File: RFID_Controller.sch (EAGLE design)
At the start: 25 parts, among them IC1 74HC595N, K1 FTR-K1C, T1 BC547, T2 BC547

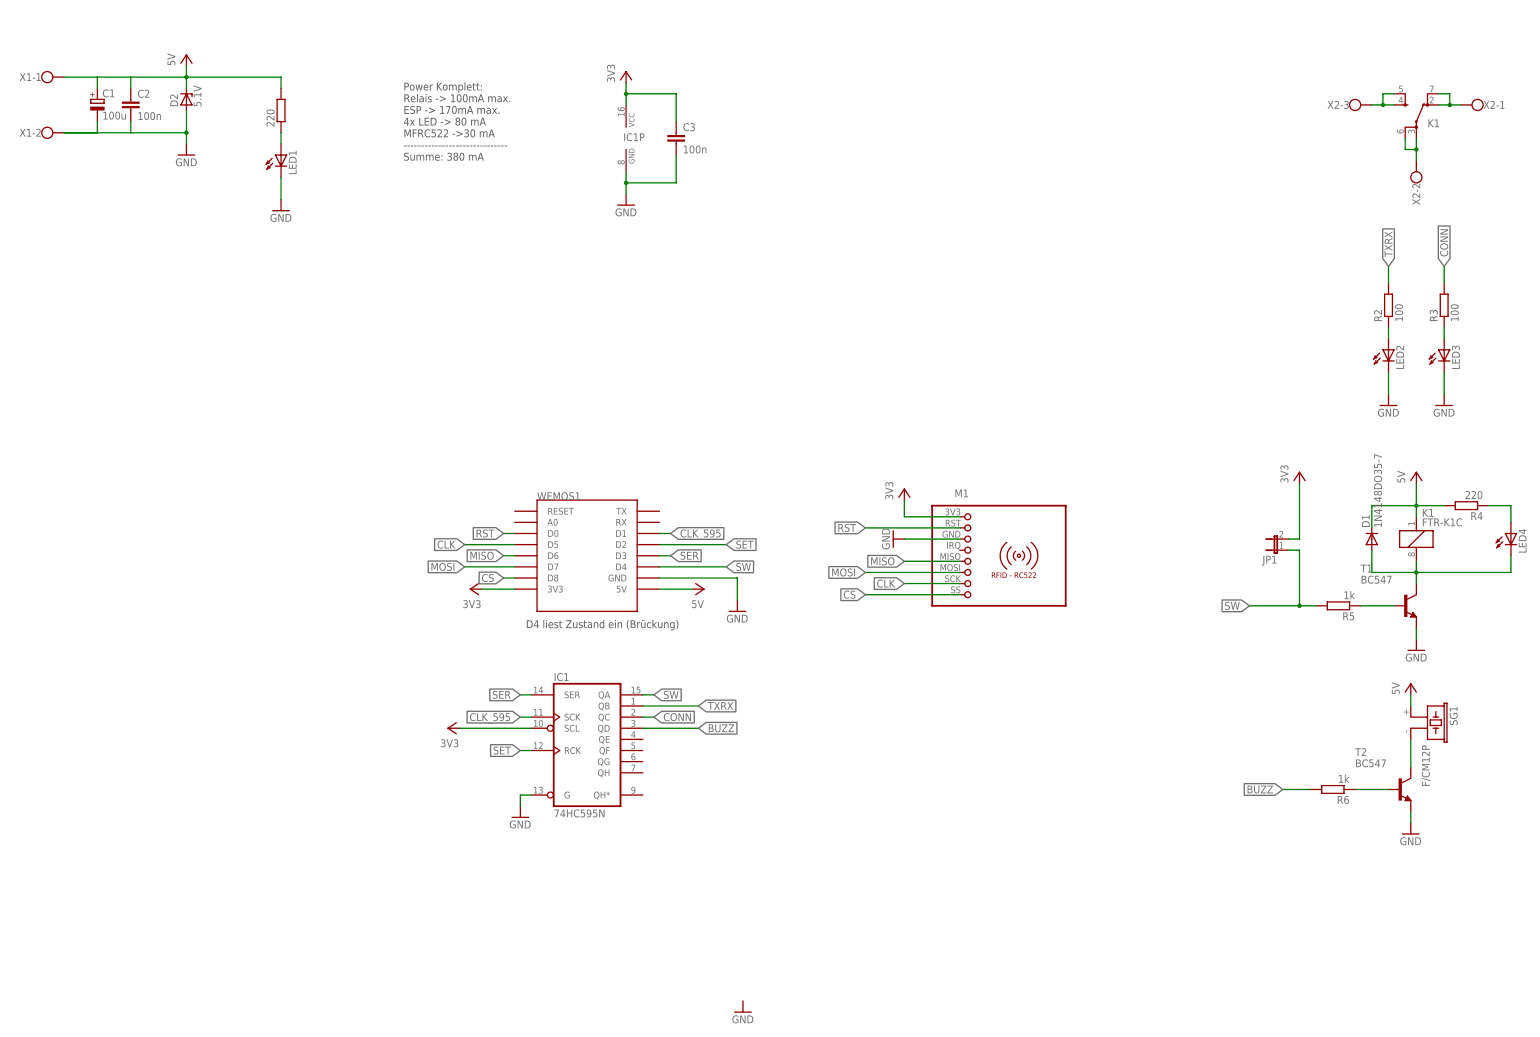
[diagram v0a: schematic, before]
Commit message: -add: I2C Expander for more GPIOs -add: input for sabotage detection ( switch for enclosure cover ) -add: 2 more inputs for possible extensions -mod: additional resistor in pull-up path of relais transistor
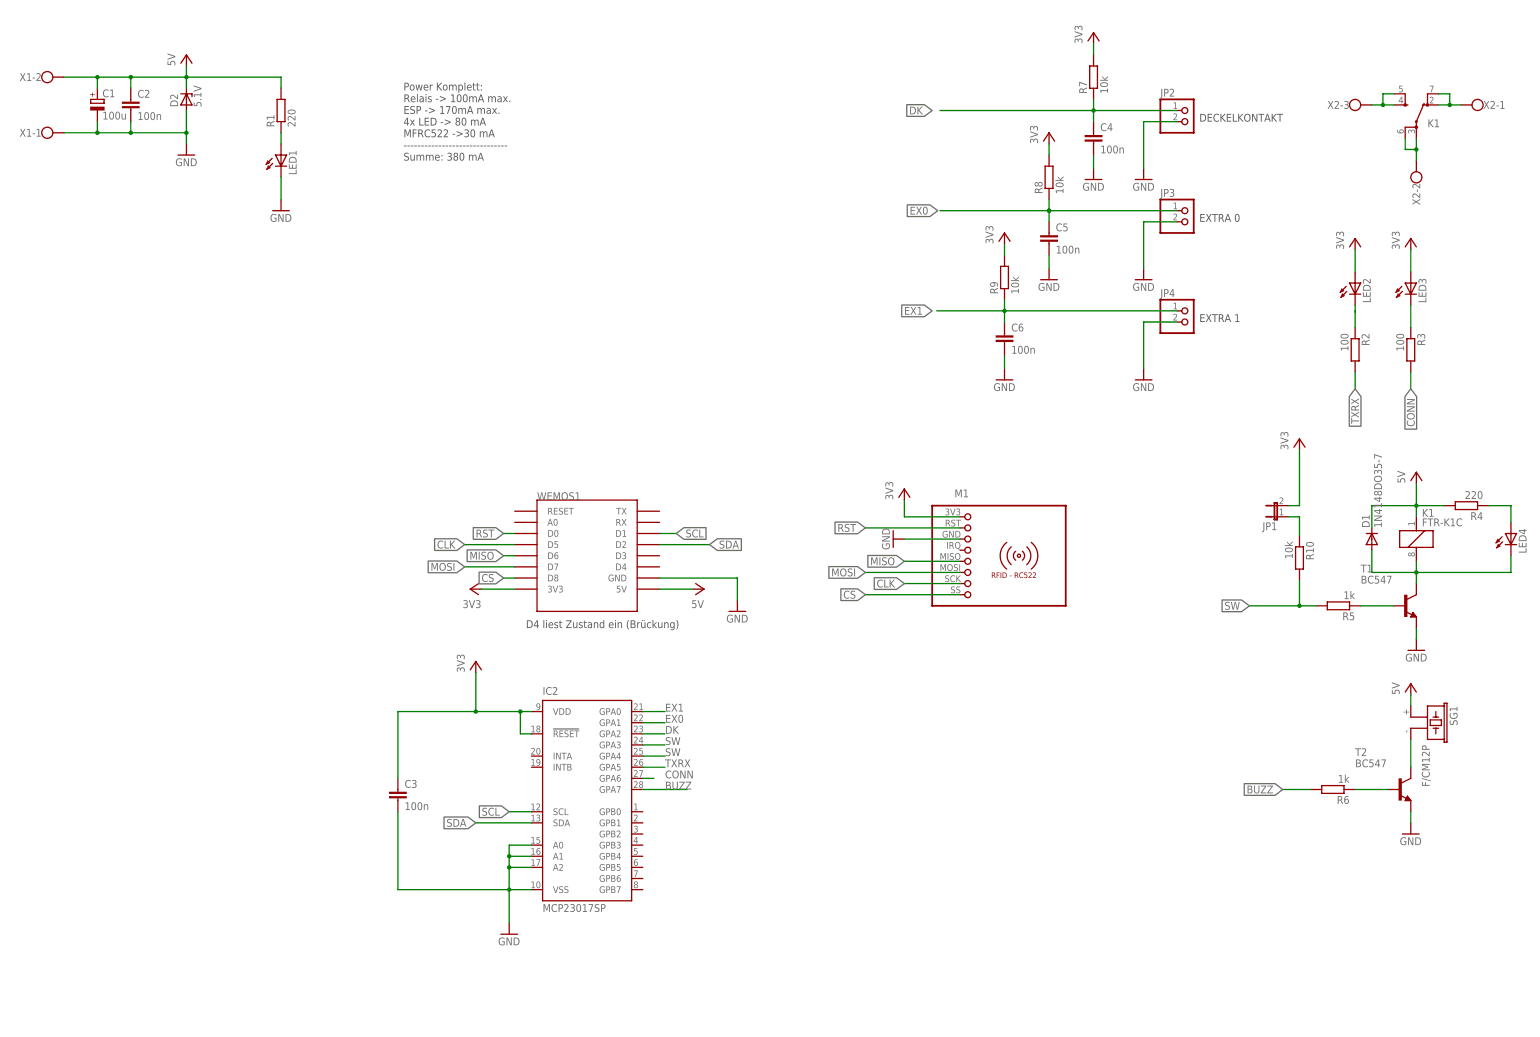
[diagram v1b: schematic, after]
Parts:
- removed IC1: 74HC595N, 74xx-eu:74HC595N
- added C4, C5, C6: 100n, rcl:C-EU050-025X075
- added IC2: MCP23017SP, microchip:MCP23017SP
- added JP2, JP3, JP4: (no value), pinhead:PINHD-1X2
- added R10, R7, R8, R9: 10k, rcl:R-EU_0204/7
- R1: value (none) -> 220
- renumbered 220 to R1
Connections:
- removed net CLK_595: IC1A.SCK, WEMOS1.D1
- removed net SER: IC1A.SER, WEMOS1.D3
- removed net SET: IC1A.RCK, WEMOS1.D2
- new net DK: C4.1, IC2.GPA2, JP2.1, R7.1
- new net EX0: C5.1, IC2.GPA1, JP3.1, R8.1
- new net EX1: C6.1, IC2.GPA0, JP4.1, R9.1
- new net N$12: JP1.1, R10.1
- new net SCL: IC2.SCL, WEMOS1.D1
- new net SDA: IC2.SDA, WEMOS1.D2
- net 3V3: now also IC2.!RESET, IC2.VDD, LED2.A, LED3.A, R7.2, R8.2, R9.2; no longer IC1A.SCL, IC1P.VCC
- net 5V: now also X1-2.KL; no longer X1-1.KL
- net BUZZ: now also IC2.GPA7; no longer IC1A.QD
- net CONN: now also IC2.GPA6; no longer IC1A.QC
- net GND: now also C4.2, C5.2, C6.2, IC2.A0, IC2.A1, IC2.A2, IC2.VSS, JP2.2, JP3.2, JP4.2, X1-1.KL; no longer IC1A.G, IC1P.GND, LED2.C, LED3.C, X1-2.KL
- net N$2: now also LED2.C; no longer LED2.A
- net N$3: now also LED3.C; no longer LED3.A
- net SW: now also IC2.GPA3, IC2.GPA4, R10.2; no longer IC1A.QA, JP1.1, WEMOS1.D4
- net TXRX: now also IC2.GPA5; no longer IC1A.QB
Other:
- note added: "DECKELKONTAKT"
- note added: "EXTRA 0"
- note added: "EXTRA 1"
- moved on the sheet: C3, JP1, LED2, LED3, R2, R3, X1-1, X1-2

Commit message: -mod: 2 additional Extra GPIO's -mod: replaced 3 single 1x2 pin headers with 2x5 pin header -mod: maximized copper area of relay contacts -info: Schematic verified by Ian Hubbertz
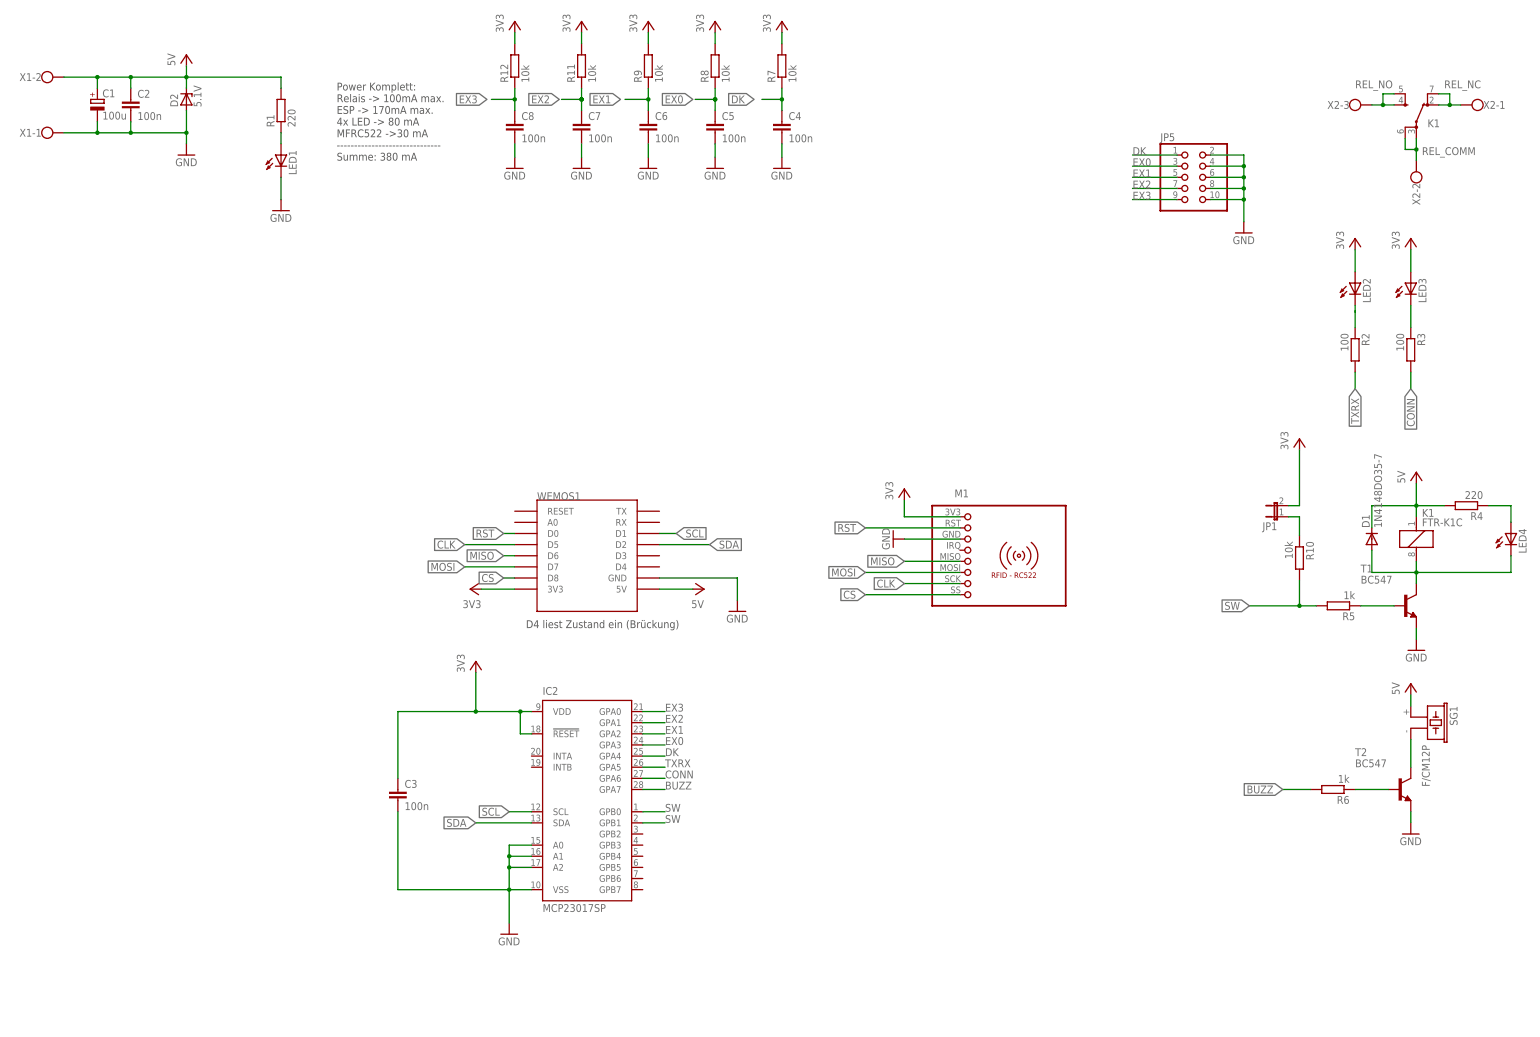
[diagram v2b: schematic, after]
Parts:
- removed JP2, JP3, JP4: (no value), pinhead:PINHD-1X2
- added C7, C8: 100n, rcl:C-EU050-025X075
- added JP5: (no value), pinhead:PINHD-2X5
- added R11, R12: 10k, rcl:R-EU_0204/7
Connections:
- net N$10 renamed REL_NC
- net N$8 renamed REL_COMM
- net N$9 renamed REL_NO
- new net EX2: C7.1, IC2.GPA1, JP5.7, R11.1
- new net EX3: C8.1, IC2.GPA0, JP5.9, R12.1
- net 3V3: now also R11.2, R12.2
- net DK: now also IC2.GPA4, JP5.1; no longer IC2.GPA2, JP2.1
- net EX0: now also IC2.GPA3, JP5.3; no longer IC2.GPA1, JP3.1
- net EX1: now also IC2.GPA2, JP5.5; no longer IC2.GPA0, JP4.1
- net GND: now also C7.2, C8.2, JP5.10, JP5.2, JP5.4, JP5.6, JP5.8; no longer JP2.2, JP3.2, JP4.2
- net SW: now also IC2.GPB0, IC2.GPB1; no longer IC2.GPA3, IC2.GPA4
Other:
- note removed: "DECKELKONTAKT"
- note removed: "EXTRA 0"
- note removed: "EXTRA 1"
- moved on the sheet: C4, C5, C6, R7, R8, R9

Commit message: -mod: modifies according to Roberts recommendations
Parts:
- added C10, C9: 100p, rcl:C-EU050-024X044
- added R13, R14: 1k, rcl:R-EU_0204/7
- R10: value 10k -> 1k
- R2, R3: value 100 -> 100R
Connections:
- removed net N$11: R5.1, T1.B
- new net N$8: IC2.GPB0, R5.2
- new net VCC: C9.1
- net 3V3: now also R13.1, R14.1
- net 5V: now also C10.1
- net GND: now also C10.2, C9.2
- net SCL: now also R13.2
- net SDA: now also R14.2
- net SW: now also R5.1, T1.B; no longer IC2.GPB0, R5.2
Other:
- moved on the sheet: R5
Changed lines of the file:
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@@
 <part name="LED3" library="led" deviceset="LED" device="3MM"/>
 <part name="LED4" library="led" deviceset="LED" device="3MM"/>
-<part name="R2" library="rcl" deviceset="R-EU_" device="0204/7" value="100"/>
-<part name="R3" library="rcl" deviceset="R-EU_" device="0204/7" value="100"/>
+<part name="R2" library="rcl" deviceset="R-EU_" device="0204/7" value="100R"/>
+<part name="R3" library="rcl" deviceset="R-EU_" device="0204/7" value="100R"/>
 <part name="R4" library="rcl" deviceset="R-EU_" device="0204/7" value="220"/>
 <part name="GND2" library="supply1" deviceset="GND" device=""/>
@@
 <part name="GND14" library="supply1" deviceset="GND" device=""/>
 <part name="GND15" library="supply1" deviceset="GND" device=""/>
-<part name="R10" library="rcl" deviceset="R-EU_" device="0204/7" value="10k"/>
+<part name="R10" library="rcl" deviceset="R-EU_" device="0204/7" value="1k"/>
 <part name="P+12" library="supply1" deviceset="VCC" device="" value="3V3"/>
 <part name="P+13" library="supply1" deviceset="VCC" device="" value="3V3"/>
@@
 <part name="GND4" library="supply1" deviceset="GND" device=""/>
 <part name="GND10" library="supply1" deviceset="GND" device=""/>
+<part name="R13" library="rcl" deviceset="R-EU_" device="0204/7" value="1k"/>
+<part name="R14" library="rcl" deviceset="R-EU_" device="0204/7" value="1k"/>
+<part name="C9" library="rcl" deviceset="C-EU" device="050-024X044" value="100p"/>
+<part name="C10" library="rcl" deviceset="C-EU" device="050-024X044" value="100p"/>
+<part name="P+16" library="supply1" deviceset="VCC" device="" value="5V"/>
+<part name="GND12" library="supply1" deviceset="GND" device=""/>
+<part name="P+17" library="supply1" deviceset="VCC" device="" value="3V3"/>
+<part name="GND13" library="supply1" deviceset="GND" device=""/>
 </parts>
 <sheets>
@@
 <instance part="D1" gate="G$1" x="326.39" y="135.89" rot="R90"/>
 <instance part="GND6" gate="1" x="336.55" y="110.49"/>
-<instance part="R5" gate="G$1" x="318.77" y="120.65" rot="R180"/>
+<instance part="R5" gate="G$1" x="170.18" y="73.66" rot="R180"/>
 <instance part="P+2" gate="VCC" x="336.55" y="151.13"/>
 <instance part="P+3" gate="VCC" x="173.99" y="124.46" smashed="yes" rot="R270">
@@
 <instance part="GND4" gate="1" x="130.81" y="220.472"/>
 <instance part="GND10" gate="1" x="297.18" y="205.74"/>
+<instance part="R13" gate="G$1" x="121.92" y="86.36" rot="R270"/>
+<instance part="R14" gate="G$1" x="129.54" y="86.36" rot="R270"/>
+<instance part="C9" gate="G$1" x="264.16" y="134.62"/>
+<instance part="C10" gate="G$1" x="99.06" y="132.08"/>
+<instance part="P+16" gate="VCC" x="99.06" y="143.51" smashed="yes">
+<attribute name="VALUE" x="101.6" y="143.51" size="1.778" layer="96" rot="R270"/>
+</instance>
+<instance part="GND12" gate="1" x="99.06" y="119.38"/>
+<instance part="P+17" gate="VCC" x="264.16" y="147.32" smashed="yes">
+<attribute name="VALUE" x="261.62" y="144.78" size="1.778" layer="96" rot="R90"/>
+</instance>
+<instance part="GND13" gate="1" x="264.16" y="120.65"/>
 </instances>
 <busses>
@@
 <pinref part="GND10" gate="1" pin="GND"/>
 </segment>
-</net>
-<net name="N$11" class="0">
-<segment>
-<pinref part="T1" gate="G$1" pin="B"/>
-<pinref part="R5" gate="G$1" pin="1"/>
-<wire x1="331.47" y1="120.65" x2="323.85" y2="120.65" width="0.1524" layer="91"/>
+<segment>
+<pinref part="C10" gate="G$1" pin="2"/>
+<wire x1="99.06" y1="127" x2="99.06" y2="121.92" width="0.1524" layer="91"/>
+<pinref part="GND12" gate="1" pin="GND"/>
+</segment>
+<segment>
+<pinref part="C9" gate="G$1" pin="2"/>
+<pinref part="GND13" gate="1" pin="GND"/>
+<wire x1="264.16" y1="129.54" x2="264.16" y2="123.19" width="0.1524" layer="91"/>
 </segment>
 </net>
@@
 <wire x1="335.28" y1="100.33" x2="335.28" y2="97.79" width="0.1524" layer="91"/>
 </segment>
+<segment>
+<pinref part="C10" gate="G$1" pin="1"/>
+<wire x1="99.06" y1="142.24" x2="99.06" y2="134.62" width="0.1524" layer="91"/>
+</segment>
 </net>
 <net name="3V3" class="0">
@@
 <pinref part="P+8" gate="VCC" pin="VCC"/>
 <wire x1="134.62" y1="96.52" x2="132.08" y2="96.52" width="0.1524" layer="91"/>
-<wire x1="132.08" y1="96.52" x2="121.92" y2="96.52" width="0.1524" layer="91"/>
+<wire x1="132.08" y1="96.52" x2="129.54" y2="96.52" width="0.1524" layer="91"/>
+<wire x1="129.54" y1="96.52" x2="121.92" y2="96.52" width="0.1524" layer="91"/>
 <wire x1="121.92" y1="96.52" x2="121.92" y2="105.41" width="0.1524" layer="91"/>
 <pinref part="IC2" gate="G$1" pin="!RESET"/>
@@
 <wire x1="104.14" y1="96.52" x2="104.14" y2="81.28" width="0.1524" layer="91"/>
 <junction x="121.92" y="96.52"/>
+<pinref part="R14" gate="G$1" pin="1"/>
+<wire x1="129.54" y1="91.44" x2="129.54" y2="96.52" width="0.1524" layer="91"/>
+<junction x="129.54" y="96.52"/>
+<pinref part="R13" gate="G$1" pin="1"/>
+<wire x1="121.92" y1="91.44" x2="121.92" y2="96.52" width="0.1524" layer="91"/>
 </segment>
 <segment>
@@
 <net name="SW" class="0">
 <segment>
-<pinref part="R5" gate="G$1" pin="2"/>
 <label x="298.45" y="120.65" size="1.778" layer="95" rot="R180" xref="yes"/>
-<wire x1="313.69" y1="120.65" x2="309.88" y2="120.65" width="0.1524" layer="91"/>
 <pinref part="R10" gate="G$1" pin="2"/>
 <wire x1="309.88" y1="120.65" x2="298.45" y2="120.65" width="0.1524" layer="91"/>
 <wire x1="309.88" y1="126.492" x2="309.88" y2="120.65" width="0.1524" layer="91"/>
+<pinref part="T1" gate="G$1" pin="B"/>
+<wire x1="309.88" y1="120.65" x2="331.47" y2="120.65" width="0.1524" layer="91"/>
 <junction x="309.88" y="120.65"/>
 </segment>
 <segment>
-<pinref part="IC2" gate="G$1" pin="GPB0"/>
-<wire x1="160.02" y1="73.66" x2="165.1" y2="73.66" width="0.1524" layer="91"/>
-<label x="165.1" y="73.66" size="1.778" layer="95"/>
-</segment>
-<segment>
 <pinref part="IC2" gate="G$1" pin="GPB1"/>
-<wire x1="160.02" y1="71.12" x2="165.1" y2="71.12" width="0.1524" layer="91"/>
-<label x="165.1" y="71.12" size="1.778" layer="95"/>
+<label x="182.88" y="73.66" size="1.778" layer="95"/>
+<pinref part="R5" gate="G$1" pin="1"/>
+<wire x1="175.26" y1="73.66" x2="180.34" y2="73.66" width="0.1524" layer="91"/>
+<wire x1="160.02" y1="71.12" x2="180.34" y2="71.12" width="0.1524" layer="91"/>
+<wire x1="180.34" y1="71.12" x2="180.34" y2="73.66" width="0.1524" layer="91"/>
+<wire x1="180.34" y1="73.66" x2="182.88" y2="73.66" width="0.1524" layer="91"/>
+<junction x="180.34" y="73.66"/>
 </segment>
 </net>
@@
 <segment>
 <pinref part="IC2" gate="G$1" pin="SCL"/>
-<wire x1="134.62" y1="73.66" x2="129.54" y2="73.66" width="0.1524" layer="91"/>
-<label x="129.54" y="73.66" size="1.778" layer="95" rot="R180" xref="yes"/>
+<wire x1="134.62" y1="73.66" x2="121.92" y2="73.66" width="0.1524" layer="91"/>
+<label x="114.3" y="73.66" size="1.778" layer="95" rot="R180" xref="yes"/>
+<pinref part="R13" gate="G$1" pin="2"/>
+<wire x1="121.92" y1="73.66" x2="114.3" y2="73.66" width="0.1524" layer="91"/>
+<wire x1="121.92" y1="81.28" x2="121.92" y2="73.66" width="0.1524" layer="91"/>
+<junction x="121.92" y="73.66"/>
 </segment>
 <segment>
@@
 <segment>
 <pinref part="IC2" gate="G$1" pin="SDA"/>
-<wire x1="134.62" y1="71.12" x2="121.92" y2="71.12" width="0.1524" layer="91"/>
+<wire x1="134.62" y1="71.12" x2="129.54" y2="71.12" width="0.1524" layer="91"/>
 <label x="121.92" y="71.12" size="1.778" layer="95" rot="R180" xref="yes"/>
+<pinref part="R14" gate="G$1" pin="2"/>
+<wire x1="129.54" y1="71.12" x2="121.92" y2="71.12" width="0.1524" layer="91"/>
+<wire x1="129.54" y1="81.28" x2="129.54" y2="71.12" width="0.1524" layer="91"/>
+<junction x="129.54" y="71.12"/>
 </segment>
 <segment>
@@
 </segment>
 </net>
+<net name="N$8" class="0">
+<segment>
+<pinref part="R5" gate="G$1" pin="2"/>
+<pinref part="IC2" gate="G$1" pin="GPB0"/>
+<wire x1="165.1" y1="73.66" x2="160.02" y2="73.66" width="0.1524" layer="91"/>
+</segment>
+</net>
+<net name="VCC" class="0">
+<segment>
+<pinref part="C9" gate="G$1" pin="1"/>
+<pinref part="P+17" gate="VCC" pin="VCC"/>
+<wire x1="264.16" y1="137.16" x2="264.16" y2="144.78" width="0.1524" layer="91"/>
+</segment>
+</net>
